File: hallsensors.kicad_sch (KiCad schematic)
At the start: 13 parts

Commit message: Minors, annotation
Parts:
- gave numbers to parts that had none: 11
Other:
- title: (none) -> RedShift-117.6-LogicBoard-F103

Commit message: Add footprints, fixed xtal
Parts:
- C36: renamed from C34; footprint Capacitor_SMD:C_0402_1005Metric -> Capacitor_SMD:C_0603_1608Metric_Pad1.08x0.95mm_HandSolder
- C37: renamed from C35; footprint Capacitor_SMD:C_0402_1005Metric -> Capacitor_SMD:C_0603_1608Metric_Pad1.08x0.95mm_HandSolder
- C38: renamed from C36; footprint Capacitor_SMD:C_0402_1005Metric -> Capacitor_SMD:C_0603_1608Metric_Pad1.08x0.95mm_HandSolder
- C39: renamed from C37; footprint Capacitor_SMD:C_0402_1005Metric -> Capacitor_SMD:C_0603_1608Metric_Pad1.08x0.95mm_HandSolder
- C40: renamed from C38; footprint Capacitor_SMD:C_0402_1005Metric -> Capacitor_SMD:C_0603_1608Metric_Pad1.08x0.95mm_HandSolder
- R32: renamed from R31; footprint (none) -> Resistor_SMD:R_0603_1608Metric_Pad0.98x0.95mm_HandSolder
- R33: renamed from R32; footprint (none) -> Resistor_SMD:R_0603_1608Metric_Pad0.98x0.95mm_HandSolder
- R34: renamed from R33; footprint (none) -> Resistor_SMD:R_0603_1608Metric_Pad0.98x0.95mm_HandSolder
- R35: renamed from R34; footprint (none) -> Resistor_SMD:R_0603_1608Metric_Pad0.98x0.95mm_HandSolder
- R36: renamed from R35; footprint (none) -> Resistor_SMD:R_0603_1608Metric_Pad0.98x0.95mm_HandSolder
- R37: renamed from R36; footprint (none) -> Resistor_SMD:R_0603_1608Metric_Pad0.98x0.95mm_HandSolder
- renumbered D6 to D7, XLED1 to X8

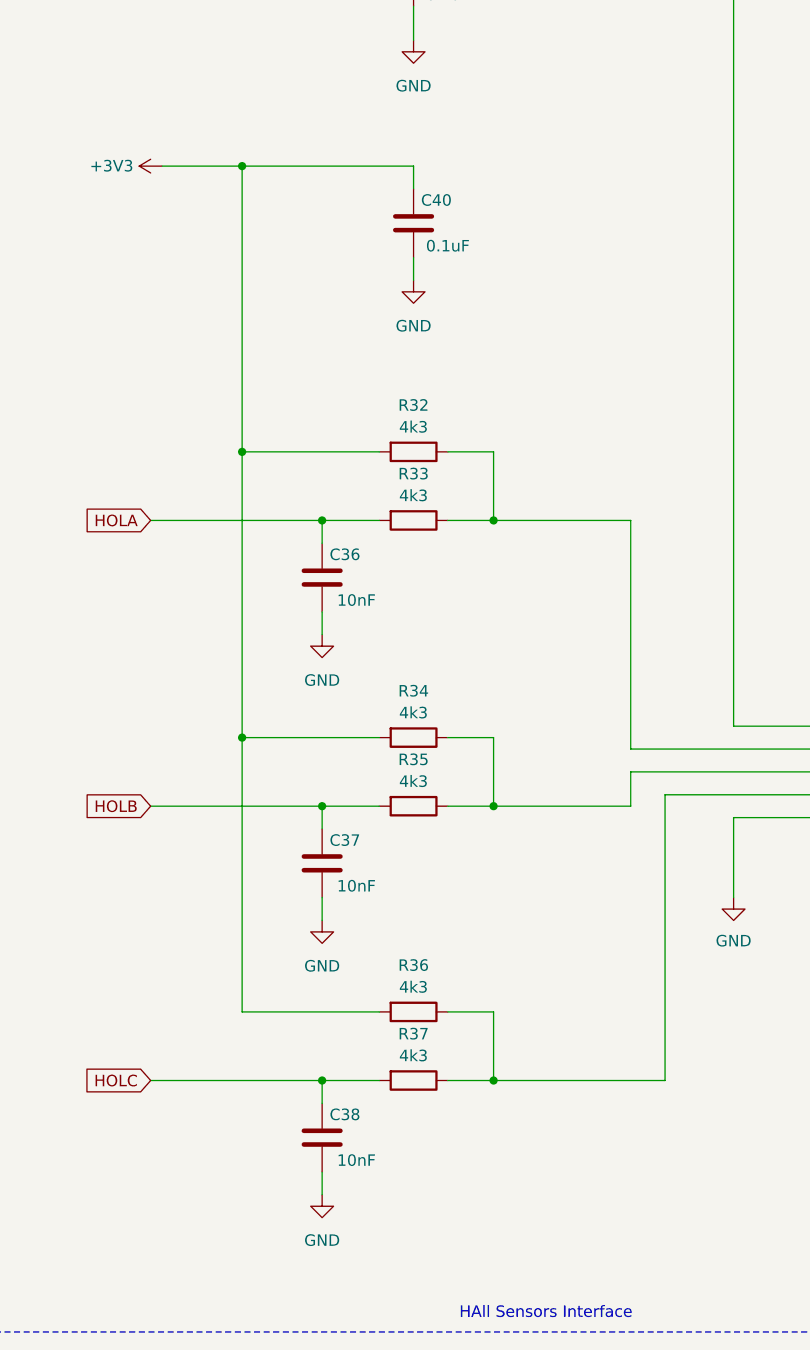
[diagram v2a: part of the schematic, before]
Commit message: Add files via upload
Add leds and minors
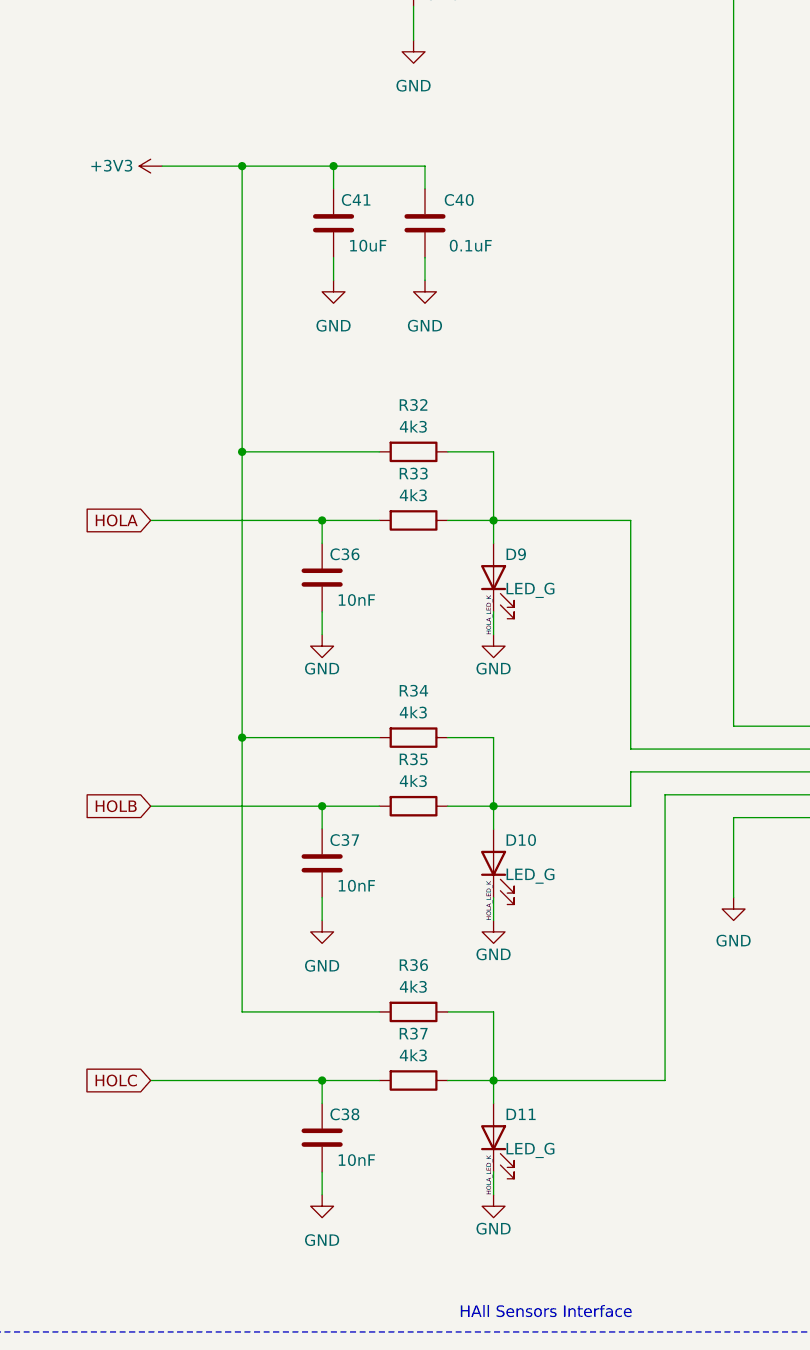
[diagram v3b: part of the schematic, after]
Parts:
- added C41: 10uF, Capacitor_SMD:C_0603_1608Metric_Pad1.08x0.95mm_HandSolder, symbol Device:C
- added D10, D11, D9: LED_G, LED_SMD:LED_0603_1608Metric, symbol Device:LED
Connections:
- net +3V3: now also C41.1
- net GND: now also C41.2, D10.1 (K), D11.1 (K), D9.1 (K)
- net at R32.1, R33.1, X8.2 (Pin_2): now also D9.2 (A)
- net at R36.1, R37.1, X8.4 (Pin_4): now also D11.2 (A)
- net at R34.1, R35.1, X8.3 (Pin_3): now also D10.2 (A)
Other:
- moved on the sheet: C40

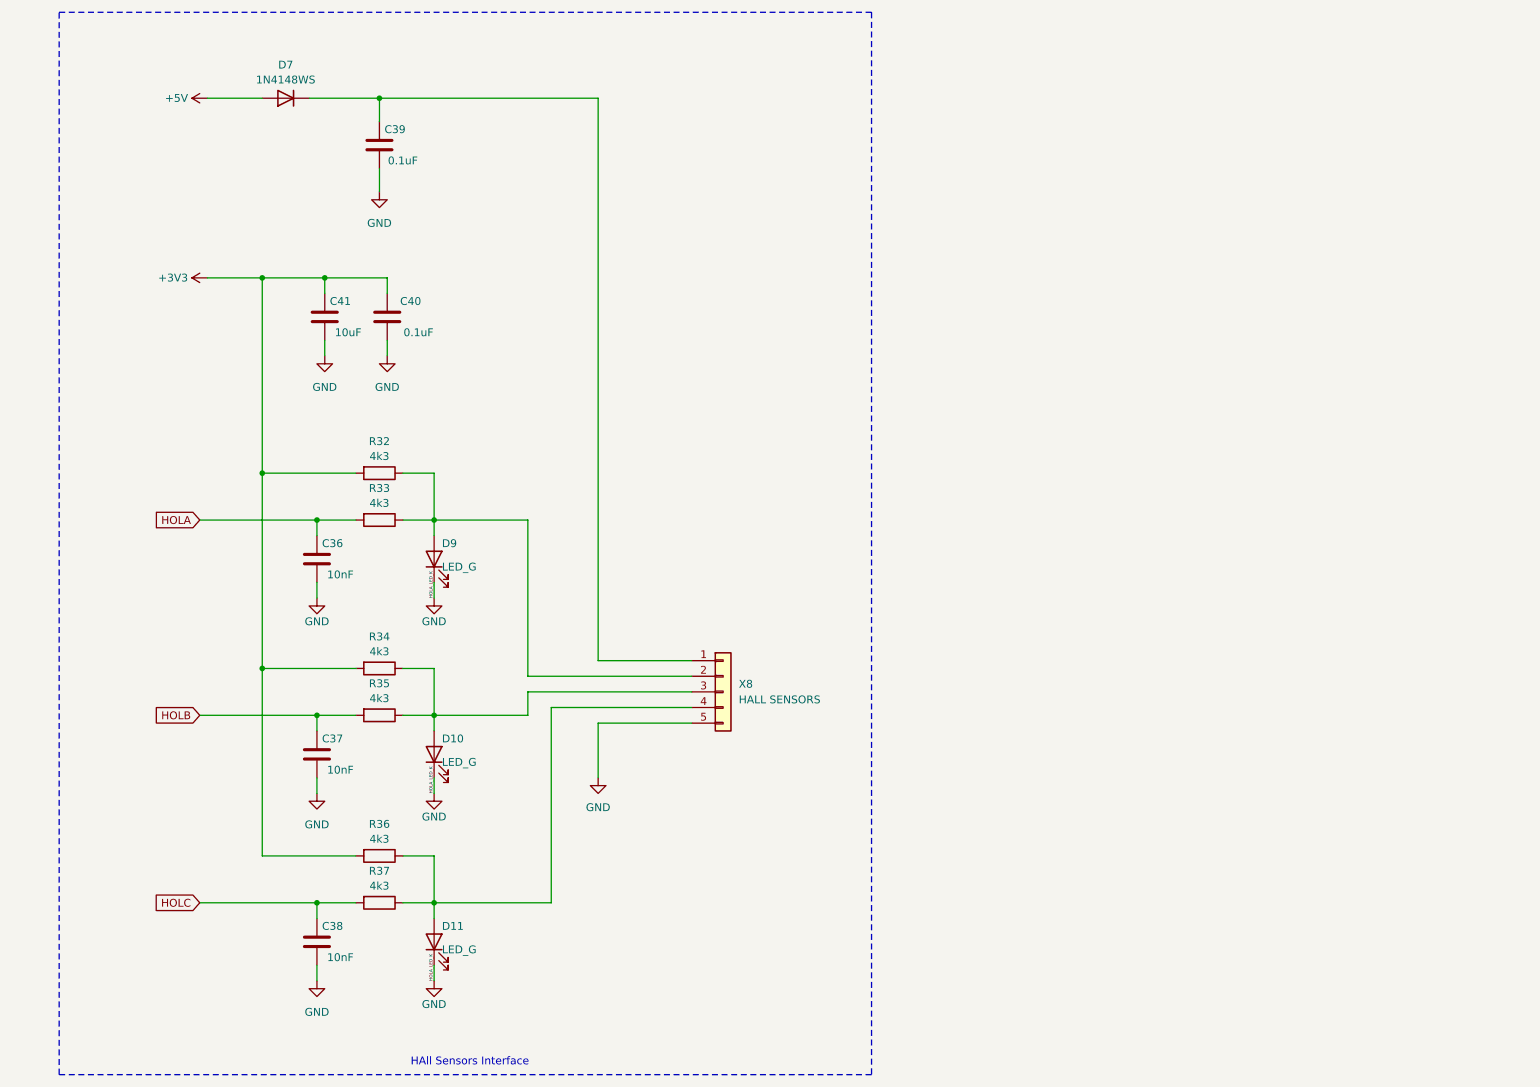
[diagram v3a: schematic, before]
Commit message: fixed some footprints
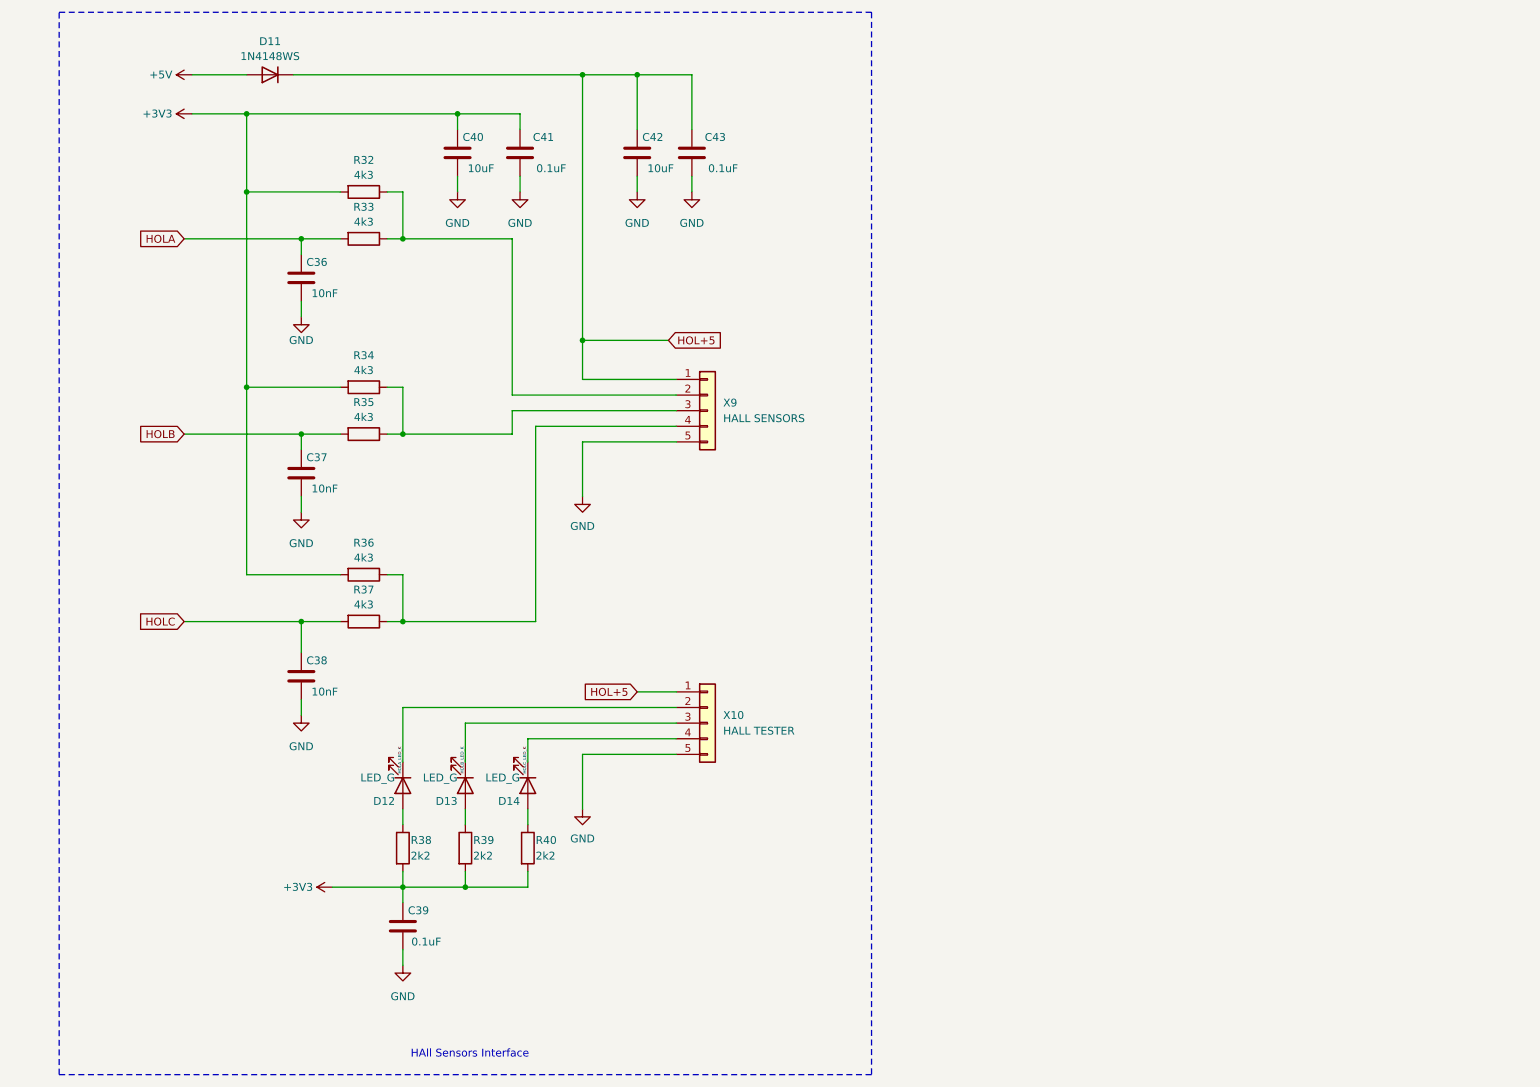
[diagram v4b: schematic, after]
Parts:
- removed D10, D11, D9: LED_G, LED_SMD:LED_0603_1608Metric, symbol Device:LED
- added C42: 10uF, Capacitor_SMD:C_0603_1608Metric_Pad1.08x0.95mm_HandSolder, symbol Device:C
- added C43: 0.1uF, Capacitor_SMD:C_0603_1608Metric_Pad1.08x0.95mm_HandSolder, symbol Device:C
- added D12, D13, D14: LED_G, LED_SMD:LED_0603_1608Metric, symbol Device:LED
- added R38, R39, R40: 2k2, Resistor_SMD:R_0603_1608Metric_Pad0.98x0.95mm_HandSolder, symbol Device:R
- added X10: HALL TESTER, symbol Connector_Generic:Conn_01x05
- renumbered C41 to C40, C40 to C41, D7 to D11, X8 to X9
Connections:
- net +3V3: now also C39.1, R38.2, R39.2, R40.2
- net GND: now also C42.2, C43.2, X10.5 (Pin_5)
- net HOL+5: now reaches D11.1 (K), X9.1 (Pin_1)
- net HOL+5: now also C42.1, C43.1, X10.1 (Pin_1); no longer C39.1
- new net: D13.2 (A), R39.1
- new net: D12.2 (A), R38.1
- new net: D14.2 (A), R40.1
- new net HOLA_LED_K: D12.1 (K), X10.2 (Pin_2)
- new net HOLB_LED_K: D13.1 (K), X10.3 (Pin_3)
- new net HOLC_LED_K: D14.1 (K), X10.4 (Pin_4)
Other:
- moved on the sheet: C36, C37, C38, C40, C41, D11, R32, R33, R34, R35, R36, R37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

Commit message: Fixed short cirquit, minors
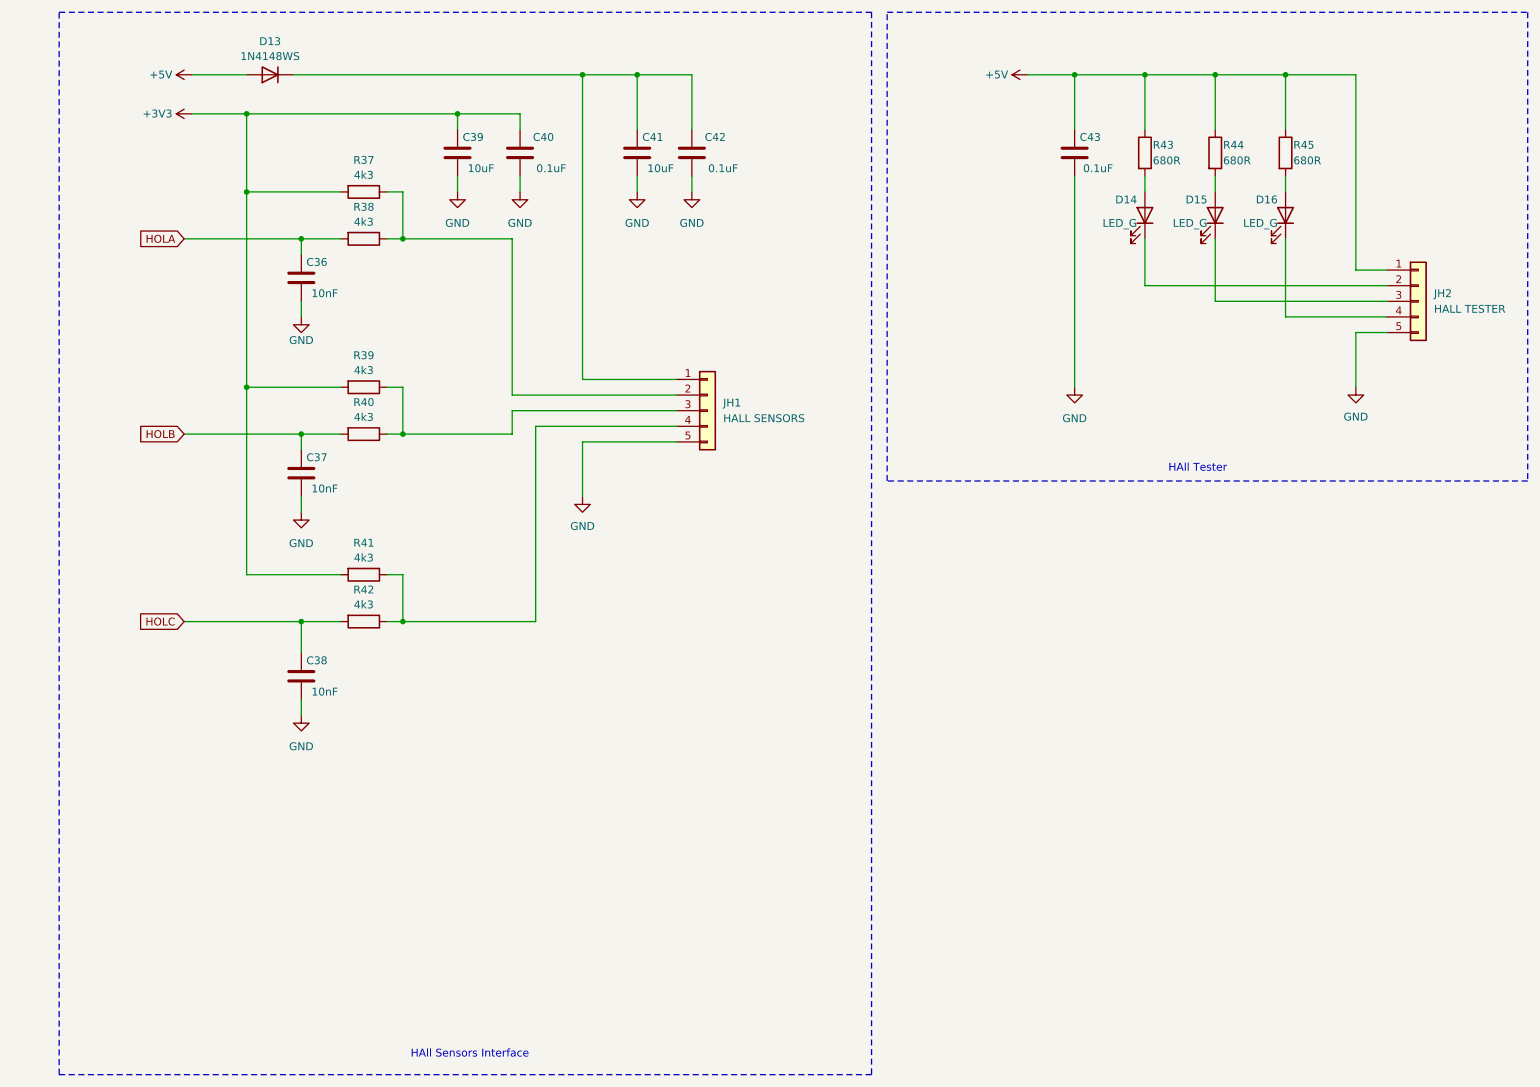
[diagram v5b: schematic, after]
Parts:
- removed D12, D13: LED_G, LED_SMD:LED_0603_1608Metric, symbol Device:LED
- removed R38, R39, R40: 2k2, Resistor_SMD:R_0603_1608Metric_Pad0.98x0.95mm_HandSolder, symbol Device:R
- added D15, D16: LED_G, LED_SMD:LED_0603_1608Metric, symbol Device:LED
- added R43, R44, R45: 680R, Resistor_SMD:R_0603_1608Metric_Pad0.98x0.95mm_HandSolder, symbol Device:R
- renumbered C40 to C39, C41 to C40, C42 to C41, C43 to C42, C39 to C43, D11 to D13, X9 to JH1, X10 to JH2, R32 to R37, R33 to R38, R34 to R39, R35 to R40, R36 to R41, R37 to R42
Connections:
- net +3V3: no longer C43.1
- net +5V: now also C43.1, JH2.1 (Pin_1), R43.1, R44.1, R45.1
- net at D14.2 (A): now also R43.2
- net HOL+5: no longer names the net of C41.1, C42.1, D13.1 (K), JH1.1 (Pin_1)
- net HOL+5: no longer JH2.1 (Pin_1)
- net HOLA_LED_K: no longer names the net of JH2.2 (Pin_2)
- net HOLA_LED_K: now also D14.1 (K)
- net HOLB_LED_K: no longer names the net of JH2.3 (Pin_3)
- net HOLB_LED_K: now also D15.1 (K)
- net HOLC_LED_K: no longer names the net of JH2.4 (Pin_4)
- net HOLC_LED_K: now also D16.1 (K); no longer D14.1 (K)
- new net: D16.2 (A), R45.2
- new net: D15.2 (A), R44.2
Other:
- note added: "HAll Tester"
- moved on the sheet: C43, JH2

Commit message: Fix mistakes
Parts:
- renumbered JH1 to XH1, JH2 to XH2
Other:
- moved on the sheet: C36, C37, C38, C39, C40, C41, C42, C43, D13, D14, D15, D16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
